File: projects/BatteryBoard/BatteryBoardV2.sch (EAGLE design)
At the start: 227 parts, among them M1 BSO201SP, SW1 BTS50015-1TAD, SW2 BTS50015-1TAD, T1 AD590FLATPACK, T2 AD590FLATPACK, T3 AD590FLATPACK, T4 AD590FLATPACK, U1 TCA9535PWR, U10 LT1962-3, U11 LT1962-3, U12 LTC4411, U13 LTC4411, U14 LTC4121, U15 VNS3NV04DP-E, U16 LTC4121, U17 VNS3NV04DP-E, U18 AD8418, U19 AD8418, U2 AD7991-0, U3 LTC4412MPS6, U4 LTC4121-4.2, U5 LTC4121-4.2, U6 LC05111C13MTTTG, U7 LC05111C13MTTTG, U8 AD8418, U9 AD8418

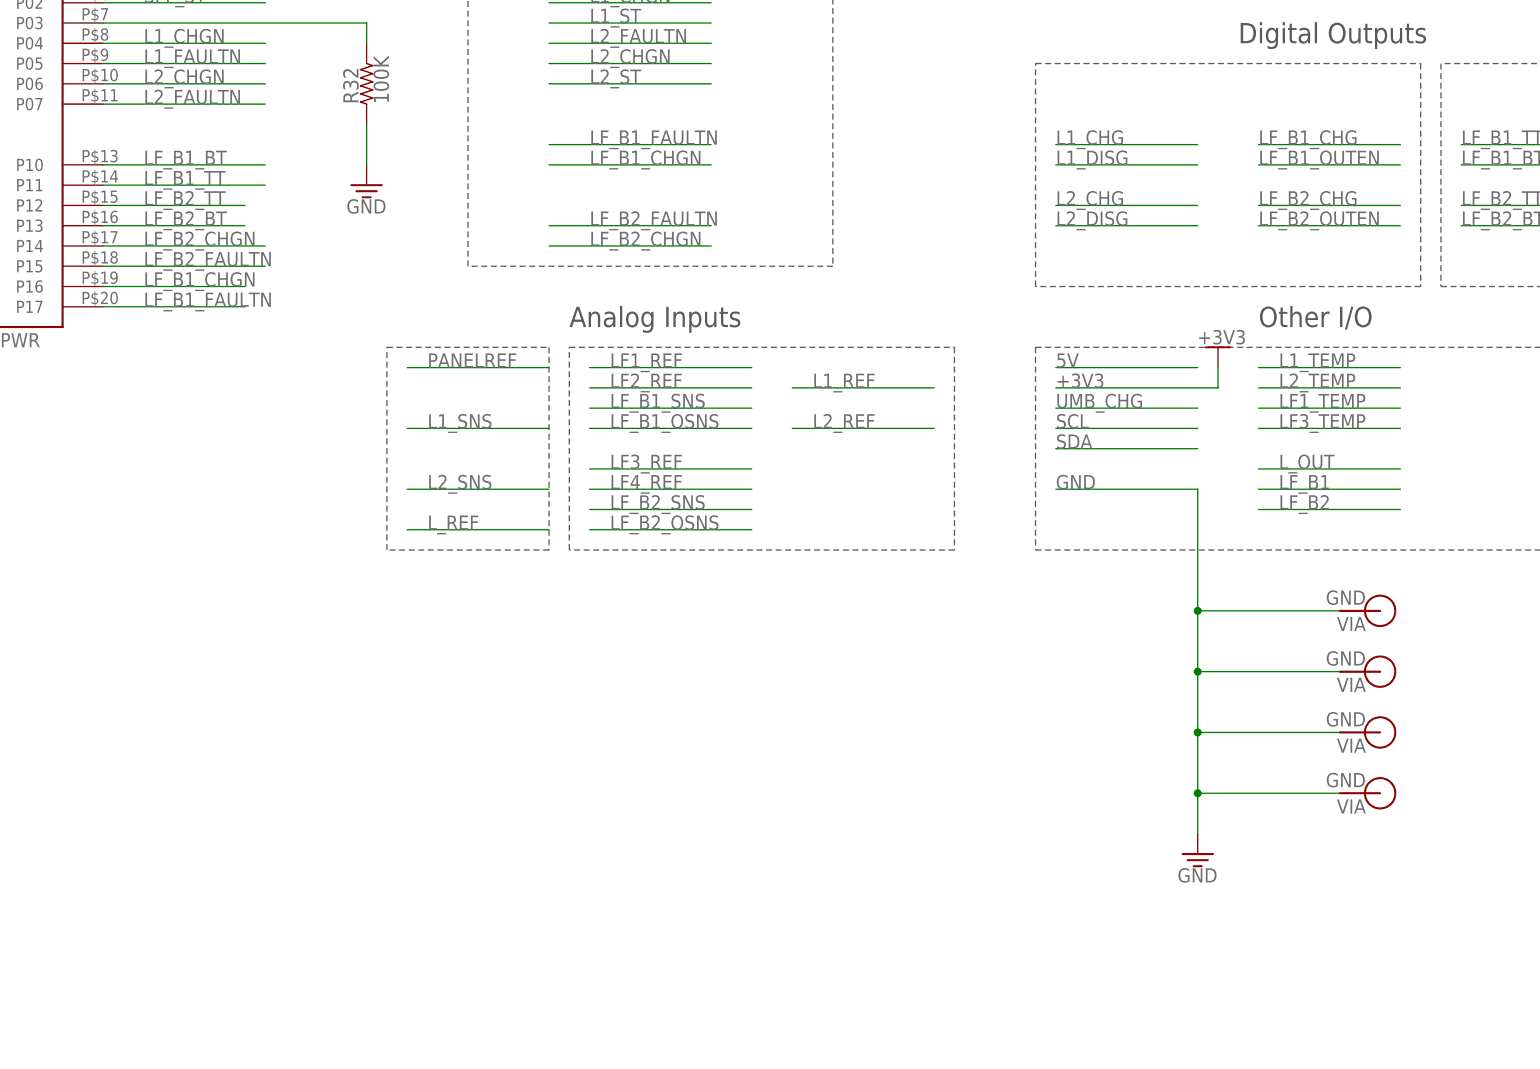
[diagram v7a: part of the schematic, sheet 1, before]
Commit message: Finished Battery Board V2. Verified all nets connected, silkscreens are readable, axes identified, no overlapping polygons. Created Gerber files, Gerber zip, and schematic pdf.
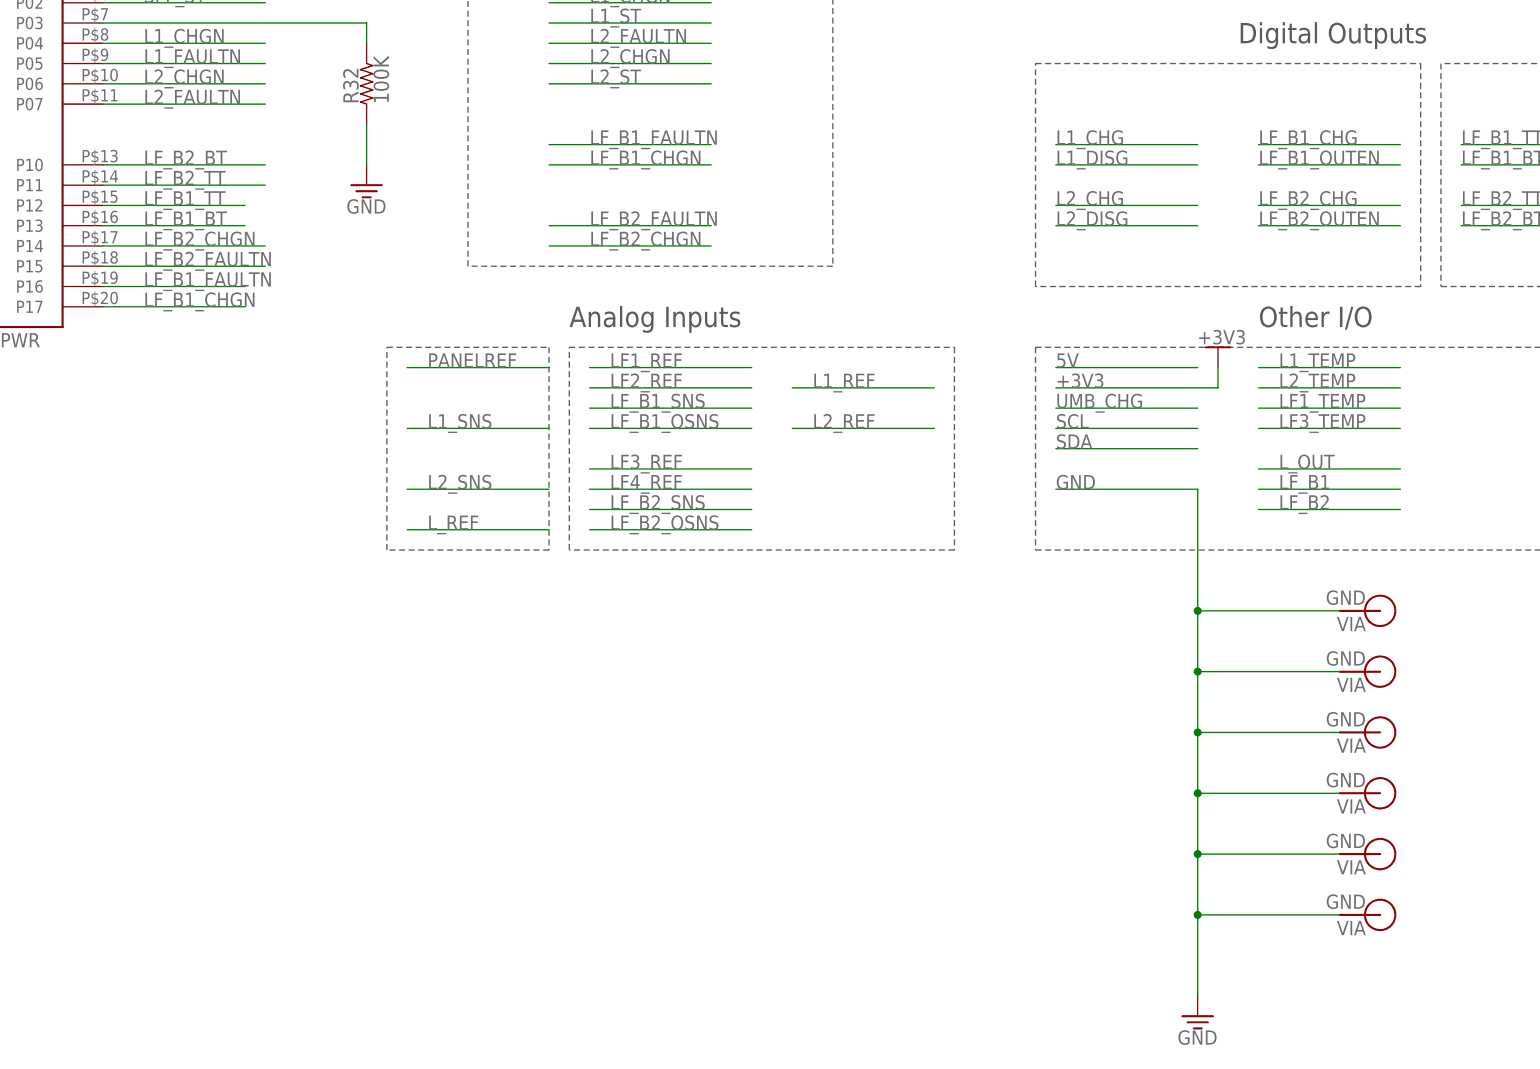
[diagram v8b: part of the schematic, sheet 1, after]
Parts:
- removed V37: LF_B1_FAULTN, BrownSpaceEngineering:VIA60MIL-SQ
- removed V38: LIFE1, BrownSpaceEngineering:VIA60MIL-SQ
- removed V39: LIFE2, BrownSpaceEngineering:VIA60MIL-SQ
- added V28: GND, BrownSpaceEngineering:VIA60MIL-SQ
- V22: value LION1_GND+ -> L1_GND+
- V23: value LION1_GND- -> L1_GND-
- V24: value LION2_GND+ -> L2_GND+
- V25: value LION2_GND- -> L2_GND-
- V32, V35: value LF_B1_CHG -> LFB1_CHG
- V36: value LF_B1_CHGN -> GND
- V43: value LF_B1_OUTEN -> LFB1_OUTEN
- V46: value LF_B1_OSNS -> LFB1_OSNS
- V47: value LF_B2_CHG -> LFB2_CHG
- V51: value LF_B2_OUTEN -> LFB2_OUTEN
- V99: value LF_B2_OSNS -> LFB2_OSNS
- renumbered $6_188_$_2017-09-09_23-53-10 to V99
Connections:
- net GND: now also V28.P$1, V36.P$1
- net LF_B1_BT: now also U1.P13; no longer U1.P10
- net LF_B1_CHGN: now also U1.P17; no longer U1.P16, V36.P$1
- net LF_B1_FAULTN: now also U1.P16; no longer U1.P17, V37.P$1
- net LF_B1_TT: now also U1.P12; no longer U1.P11
- net LF_B2_BT: now also U1.P10; no longer U1.P13
- net LF_B2_TT: now also U1.P11; no longer U1.P12
- net LIFE1: no longer V38.P$1
- net LIFE2: no longer V39.P$1
